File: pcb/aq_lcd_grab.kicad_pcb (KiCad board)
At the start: 2 copper layers, 52.1 x 60.8 mm, 2 parts, among them J1 Conn_01x39_Socket, J2 Conn_01x39_Socket

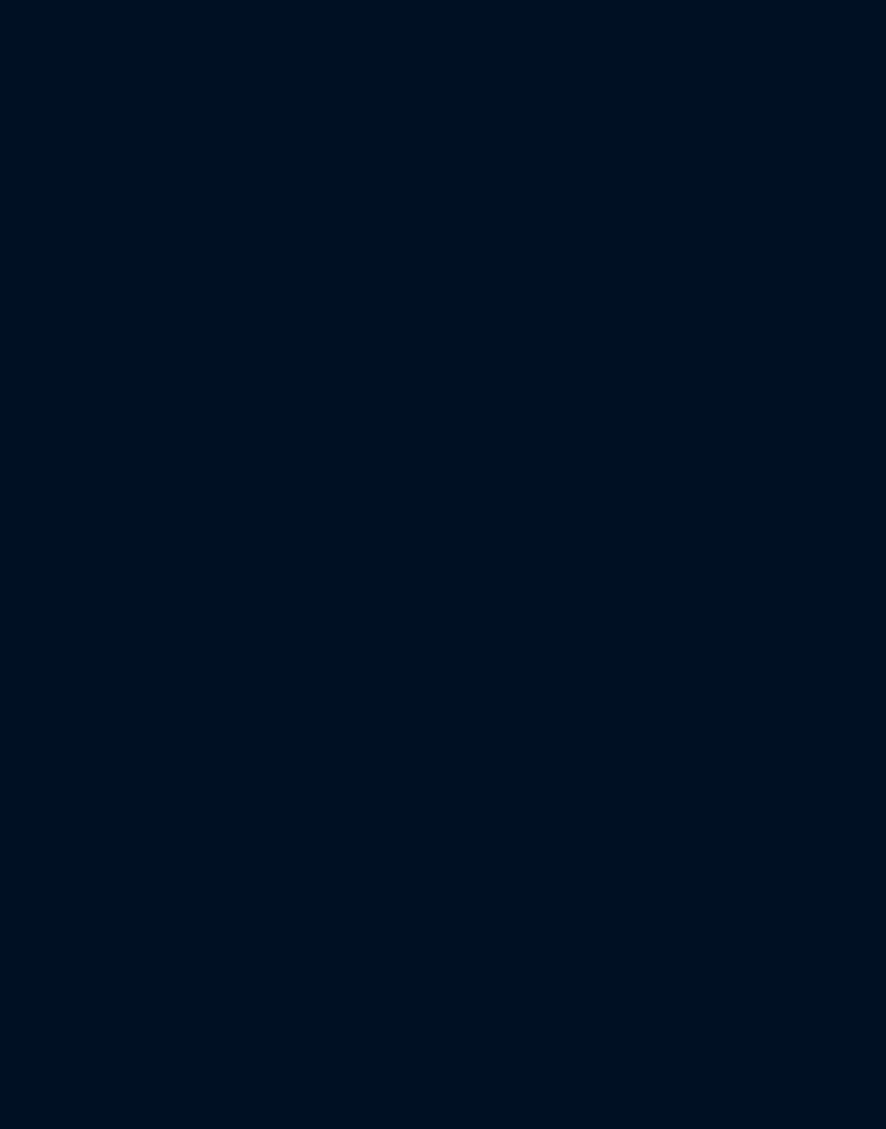
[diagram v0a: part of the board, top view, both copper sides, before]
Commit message: Add RP2350A to schematic, mirroring RPi minimal-board reference
Build out the SKiDL netlist with the RP2350A core and its supporting
components (decoupling, SMPS inductor, crystal, USB recovery header,
status LED, bring-up test points, 3-pin target power connector).

Components, values, and per-rail decoupling match Raspberry Pi's
official "RP2350 Minimal Board" KiCad design 1:1 where possible:
  - RP2350_60QFN symbol + custom QFN-60 ThermalVias footprint
  - L1 = 3.3 µH polarised AOTA-B201610S3R3-101-T on L_pol_2016
  - Y1 = ABM8-272-T3 12 MHz crystal, 15 pF load caps
  - C1/C2  ADC_AVDD bulk + HF (no ferrite, per RPi)
  - C5     VREG_VIN input (10 µF, 0805)
  - C6/C7  +1V1 bulk near L1 on the small_pads 0402 footprint
  - C8-C11 +1V1 HF decoupling
  - C9     VREG_AVDD decoupling
  - C12-C17 6× IOVDD decoupling (one cap per pin)
  - C18    extra +1V1 HF decoupling
  - C19/C20 QSPI_IOVDD / USB_OTP_VDD decoupling (our additions)
  - R2     XOUT damping (1 kΩ, in series between U1 pin 22 and Y1)
  - R4     RUN pull-up (1 kΩ)
  - R5     VREG_AVDD filter (33 Ω)
  - R7/R8  USB D±  series (27 Ω)
  - R20    QSPI_SD1 UART-boot pull-up (our addition)
  - R21    LED current limit (our addition)

Refdes mapping intentionally matches RPi's where the same component
plays the same role, so RPi's PCB layout for the U1 cluster can be
copy-pasted into ours.

Project-local sym-lib-table and fp-lib-table register the RPi symbol
file (MCU_RaspberryPi_RP2350.kicad_sym) and footprint library
(RP2350_60QFN_minimal.pretty/) — both copied from the upstream
Minimal-KiCAD.zip archive into pcb/ so the project builds standalone
without depending on the reference/ scratch folder.

.gitignore now skips reference/ (where the upstream archive is
unpacked locally for browsing in KiCanvas / KiCad).

docs/pcb_spec.md gains a Q7b section recording RPi's design-guide
recommendations (polarised inductor, ABM8 crystal, layout review).

Co-Authored-By: Claude Opus 4.7 (1M context) <noreply@anthropic.com>
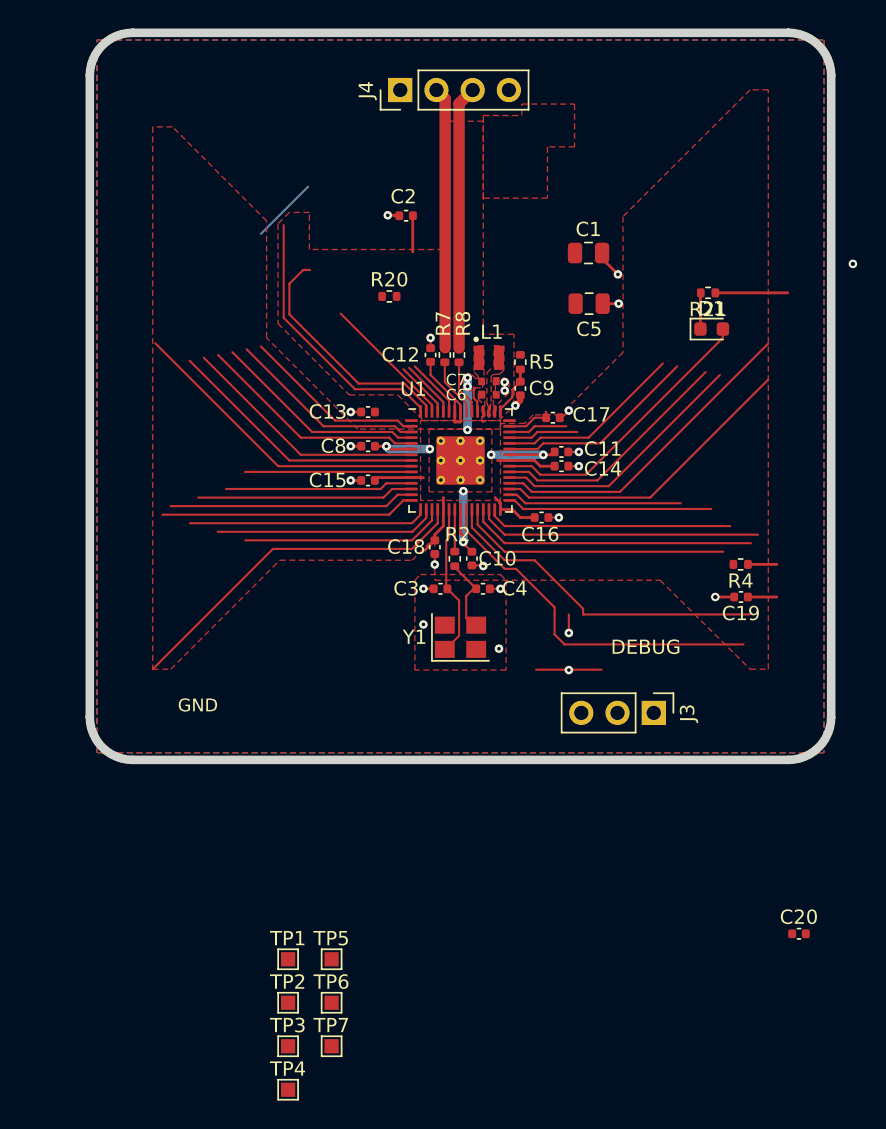
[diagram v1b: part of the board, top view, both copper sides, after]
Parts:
- added C1: 10u, Capacitor_SMD:C_0805_2012Metric, F.Cu at (230.9, 55.1)
- added C10: 4.7u, Capacitor_SMD:C_0402_1005Metric, F.Cu at (222.7, 76.6)
- added C11: 100n, Capacitor_SMD:C_0402_1005Metric, F.Cu at (229.0, 69.1)
- added C12: 100n, Capacitor_SMD:C_0402_1005Metric, F.Cu at (219.8, 62.3)
- added C13: 100n, Capacitor_SMD:C_0402_1005Metric, F.Cu at (215.4, 66.3)
- added C14: 100n, Capacitor_SMD:C_0402_1005Metric, F.Cu at (229.0, 70.1)
- added C15: 100n, Capacitor_SMD:C_0402_1005Metric, F.Cu at (215.4, 71.1)
- added C16: 100n, Capacitor_SMD:C_0402_1005Metric, F.Cu at (227.6, 73.7)
- added C17: 100n, Capacitor_SMD:C_0402_1005Metric, F.Cu at (228.4, 66.7)
- added C18: 100n, Capacitor_SMD:C_0402_1005Metric, F.Cu at (220.1, 75.8)
- added C19: 100n, Capacitor_SMD:C_0402_1005Metric, F.Cu at (241.6, 79.2)
- added C2: 100n, Capacitor_SMD:C_0402_1005Metric, F.Cu at (218.1, 52.5)
- added C20: 100n, Capacitor_SMD:C_0402_1005Metric, F.Cu at (245.6, 102.9)
- added C3: 15p, Capacitor_SMD:C_0402_1005Metric, F.Cu at (220.5, 78.7)
- added C4: 15p, Capacitor_SMD:C_0402_1005Metric, F.Cu at (223.5, 78.7)
- added C5: 10u, Capacitor_SMD:C_0805_2012Metric, F.Cu at (230.9, 58.7)
- added C6: 4.7u, RP2350_60QFN_minimal:C_0402_1005Metric_small_pads, F.Cu at (223.9, 65.1)
- added C7: 4.7u, RP2350_60QFN_minimal:C_0402_1005Metric_small_pads, F.Cu at (223.9, 64.1)
- added C8: 100n, Capacitor_SMD:C_0402_1005Metric, F.Cu at (215.4, 68.7)
- added C9: 4.7u, Capacitor_SMD:C_0402_1005Metric, F.Cu at (226.1, 64.6)
- added D1: GREEN, LED_SMD:LED_0603_1608Metric, F.Cu at (239.5, 60.5)
- added J3: Conn_01x03_Socket, Connector_PinHeader_2.54mm:PinHeader_1x03_P2.54mm_Vertical, F.Cu at (235.5, 87.4)
- added J4: Conn_01x04_Socket, Connector_PinHeader_2.54mm:PinHeader_1x04_P2.54mm_Vertical, F.Cu at (217.7, 43.7)
- added L1: 3.3u, RP2350_60QFN_minimal:L_pol_2016, F.Cu at (223.9, 62.5)
- added R2: 1k, Resistor_SMD:R_0402_1005Metric, F.Cu at (221.5, 76.6)
- added R20: 1k, Resistor_SMD:R_0402_1005Metric, F.Cu at (216.9, 58.2)
- added R21: 1k, Resistor_SMD:R_0402_1005Metric, F.Cu at (239.3, 57.9)
- added R4: 1k, Resistor_SMD:R_0402_1005Metric, F.Cu at (241.6, 77.0)
- added R5: 33, Resistor_SMD:R_0402_1005Metric, F.Cu at (226.1, 62.8)
- added R7: 27, Resistor_SMD:R_0402_1005Metric, F.Cu at (220.8, 62.3)
- added R8: 27, Resistor_SMD:R_0402_1005Metric, F.Cu at (221.8, 62.3)
- added TP1: TestPoint, TestPoint:TestPoint_Pad_1.0x1.0mm, F.Cu at (209.8, 104.7)
- added TP2: TestPoint, TestPoint:TestPoint_Pad_1.0x1.0mm, F.Cu at (209.8, 107.7)
- added TP3: TestPoint, TestPoint:TestPoint_Pad_1.0x1.0mm, F.Cu at (209.8, 110.8)
- added TP4: TestPoint, TestPoint:TestPoint_Pad_1.0x1.0mm, F.Cu at (209.8, 113.8)
- added TP5: TestPoint, TestPoint:TestPoint_Pad_1.0x1.0mm, F.Cu at (212.9, 104.7)
- added TP6: TestPoint, TestPoint:TestPoint_Pad_1.0x1.0mm, F.Cu at (212.9, 107.7)
- added TP7: TestPoint, TestPoint:TestPoint_Pad_1.0x1.0mm, F.Cu at (212.9, 110.8)
- added U1: RP2350_60QFN, RP2350_60QFN_minimal:RP2350-QFN-60-1EP_7x7_P0.4mm_EP3.4x3.4mm_ThermalVias, F.Cu at (221.9, 69.7)
- added Y1: ABM8-272-T3, Crystal:Crystal_SMD_3225-4Pin_3.2x2.5mm, F.Cu at (221.9, 82.1)
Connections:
- net /CS renamed CS
- net /DB0 renamed DB0
- net /DB1 renamed DB1
- net /DB10 renamed DB10
- net /DB11 renamed DB11
- net /DB12 renamed DB12
- net /DB13 renamed DB13
- net /DB14 renamed DB14
- net /DB15 renamed DB15
- net /DB2 renamed DB2
- net /DB3 renamed DB3
- net /DB4 renamed DB4
- net /DB5 renamed DB5
- net /DB6 renamed DB6
- net /DB7 renamed DB7
- net /DB8 renamed DB8
- net /DB9 renamed DB9
- net /DC renamed DC
- net /GND_1 renamed GND_1
- net /GND_18 renamed GND_18
- net /GND_19 renamed GND_19
- net /P20_RD renamed P20_RD
- net /P21 renamed P21
- net /P25 renamed P25
- net /P26 renamed P26
- net /P27 renamed P27
- net /P28 renamed P28
- net /P29 renamed P29
- net /P30 renamed P30
- net /P31 renamed P31
- net /P32 renamed P32
- net /P34 renamed P34
- net /P38 renamed P38
- net /P39 renamed P39
- net /VCC_33 renamed VCC_33
- net /VCC_35 renamed VCC_35
- net /VCC_36 renamed VCC_36
- net /VCC_37 renamed VCC_37
- net /WR renamed WR
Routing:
- net (no net): track 0.00 -> 372.7 mm, vias 0 -> 1
- net +3V3: track 0.00 -> 41.7 mm
- net GND: track 0.00 -> 40.2 mm, vias 0 -> 22
- net SWCLK: track 0.00 -> 25.3 mm
- net +1V1: track 0.00 -> 25.0 mm, vias 0 -> 9
- net SWDIO: track 0.00 -> 23.5 mm
- net USB_DP: track 0.00 -> 23.0 mm, vias 0 -> 1
- net GPIO22: track 0.00 -> 22.7 mm
- net GPIO21: track 0.00 -> 21.8 mm
- net LED_STATUS: track 0.00 -> 19.8 mm
- net RUN: track 0.00 -> 19.1 mm
- net USB_DM: track 0.00 -> 18.5 mm
- net GPIO23: track 0.00 -> 18.2 mm
- net N$1: track 0.00 -> 16.7 mm
- net GPIO19: track 0.00 -> 14.4 mm
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- added copper zone on F.Cu, net +1V1
- added copper zone on F.Cu, net +3V3
- added copper zone on B.Cu, net GND
- added copper zone on F.Cu, net GND
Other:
- board size 52.1 x 60.8 mm -> 170.4 x 70.2 mm
- rule pad_to_mask_clearance: 0 -> 0.051
- board text added: "DEBUG"
- board text added: "GND"

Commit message: Wire Xiao ESP32-C6 into netlist (UART boot loader + PIC32 reset)
Adds U2 (Xiao ESP32-C6 DIP module) to the SKiDL netlist with the
core control signals defined in the PCB spec:

  - GPIO16 / GPIO17 (UART0 TX/RX) -> RP2350 QSPI_SD3 / SD2 for 1 Mbaud
    UART boot loading; remuxes to RP2350 PL011 UART0 (F11 alt) at runtime
  - GPIO0  -> RP2350 RUN (push-pull; R4 supplies the pull-up)
  - GPIO1  -> PIC32 reset on J3 pin 3 (open-drain; main board pull-up)
  - 3V3 backfeed on pad 12 (bypasses Xiao's onboard LDO)
  - 5V / VBUS tied to the USB recovery header rail

Adds 22 uF + 100 uF bulk caps at the Xiao 3V3 input (C30/C31) to
absorb WiFi TX transients locally instead of pushing them onto the
target 3V3 rail (spec Q6/Q7 mitigation).

Footprint comes from a locally-tweaked SnapEDA Xiao-ESP32-C6-DIP
shipped as a project-local pretty library, mirroring the way the
RP2350 minimal-board parts are vendored.

J3 pin 3 graduates from "reserved/floating" to a real PIC32_RESET
net now that there's an ESP32 GPIO to drive it.

Co-Authored-By: Claude Opus 4.7 (1M context) <noreply@anthropic.com>
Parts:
- removed C19, C20: 100n, Capacitor_SMD:C_0402_1005Metric
- removed TP6, TP7: TestPoint, TestPoint:TestPoint_Pad_1.0x1.0mm
- added C30: 22u, Capacitor_SMD:C_0805_2012Metric, F.Cu at (256.7, 89.2)
- added C31: 100u, Capacitor_SMD:C_1206_3216Metric, F.Cu at (257.3, 86.0)
- added J5: Conn_01x03_Pin, Connector_PinHeader_2.54mm:PinHeader_1x03_P2.54mm_Vertical, F.Cu at (231.9, 86.6)
- added U2: Conn_01x14, esp32c6:XIAO-ESP32-C6-DIP, B.Cu at (221.0, 68.6)
- moved J1 107.8 mm to (174.5, 136.9), turned to 0 degrees
- moved J2 57.3 mm to (173.9, 106.7), turned to 180 degrees
- moved J3 24.1 mm to (211.3, 86.9)
- moved TP5 12.2 mm to (224.2, 100.0)
- moved TP2 11.2 mm to (217.4, 99.4)
- moved TP3 9.06 mm to (205.4, 102.8)
- moved TP4 8.50 mm to (210.1, 105.3)
- moved TP1 8.12 mm to (205.9, 97.5)
- moved C17 1.59 mm to (227.1, 67.6)
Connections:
- J3 pad 3: (no net) -> PIC32_RESET
- TP1 pad 1: SWCLK -> GPIO19
- TP2 pad 1: SWDIO -> GPIO20
- TP3 pad 1: GPIO19 -> GPIO21
- TP4 pad 1: GPIO20 -> GPIO22
- TP5 pad 1: GPIO21 -> GPIO23
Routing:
- net (no net): track 372.7 -> 197.2 mm, vias 1 -> 0
- net GND: track 40.2 -> 106.6 mm
- net GND_1: track 65.9 -> 2.80 mm
- net DB1: track 59.2 -> 3.52 mm
- net P39: track 57.1 -> 2.80 mm
- net DB0: track 53.9 -> 0.00 mm
- net PIC32_RESET: track 0.00 -> 51.9 mm
- net P38: track 51.6 -> 0.02 mm
- net DB3: track 62.7 -> 12.6 mm
- net DB2: track 51.3 -> 2.10 mm
- net VCC_37: track 61.1 -> 14.2 mm
- net VCC_36: track 50.0 -> 4.52 mm
- net DB5: track 55.5 -> 10.9 mm
- net DB4: track 49.5 -> 5.74 mm
- net VCC_35: track 53.9 -> 12.5 mm
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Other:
- board size 170.4 x 70.2 mm -> 95.5 x 102 mm
- copper layers 2 -> 4
- board text removed: "GND"

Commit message: Match RP2350 decoupling network exactly to RPi reference
Rewrites the decoupling block to mirror the Raspberry Pi RP2350
"Minimal Board" reference design (reference/RP2350A_Minimal/) 1:1.
The previous version had drifted in several ways while I wired in
the ESP32 and tried to "approximate" the reference roles -- enough
mistakes accumulated that an audit and rewrite was simpler than
patching individual pins.

Bugs fixed:
  - Pad 6 (DVDD #1) was dangling; now tied to +1V1.
  - Pad 23 (DVDD #2) was on VREG_AVDD (via the decouple() helper);
    now on +1V1 alongside pads 6 and 39.
  - C18 was a 100 nF on VREG_AVDD; reference puts it on +3V3 as a
    generic bypass. VREG_AVDD has no HF cap in the reference, only
    the 4.7 µF C9.
  - C6 was on +1V1; reference puts it on +3V3 as the pre-L1 input
    bulk near VREG_VIN.
  - C9 was bridged between VREG_AVDD and pad 23 (via decouple()
    helper). C9 is a standalone rail cap on VREG_AVDD in the
    reference, untouched by any chip pad.
  - L1 pin 1/2 were swapped relative to the reference. Pin 1 is
    the +1V1 (output) side, pin 2 the VREG_LX (switching) side --
    matters for the silkscreen dot on the polarised AOTA-B201610S3R3.
  - C19 (10 µF on +3V3, rail bulk near U1) was missing entirely.

Refdes that don't appear in our design (because we don't have RPi's
onboard 3V3 regulator or QSPI flash): C1, C2, C5. Our 10 µF +3V3
bulk now lives on C19 (matching the reference), not C5 or C1.

All other rails (XIN/XOUT/+3V3/+1V1/VREG_AVDD/VREG_LX) now match
the reference netlist node-for-node.

Includes the layout-side changes (4-layer stackup, test point
repositioning, footprint imports for the ESP32 + new caps) that
piled up in the .kicad_pcb during this work.

Co-Authored-By: Claude Opus 4.7 (1M context) <noreply@anthropic.com>
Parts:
- removed C1, C5: 10u, Capacitor_SMD:C_0805_2012Metric
- removed C2: 100n, Capacitor_SMD:C_0402_1005Metric
- added C17: 100n, Capacitor_SMD:C_0402_1005Metric, F.Cu at (53.9, 57.0)
- added C19: 10u, Capacitor_SMD:C_0805_2012Metric, F.Cu at (40.0, 49.8)
- moved R4 203.2 mm to (40.6, 46.8), turned to 0 degrees
- moved D1 196.9 mm to (42.7, 63.3), turned to 180 degrees
- moved R21 196.5 mm to (42.9, 65.9), turned to 0 degrees
- moved TP2 189.5 mm to (32.0, 59.9)
- moved C31 188.4 mm to (71.0, 113.5)
- moved J5 184.4 mm to (53.3, 40.6), turned to 0 degrees
- moved TP4 183.9 mm to (33.3, 54.6)
- moved C14 176.5 mm to (53.2, 53.7), turned to 180 degrees
- moved C11 176.3 mm to (53.2, 54.7), turned to 180 degrees
- moved C16 174.2 mm to (55.0, 49.9), turned to 180 degrees
- moved C9 170.3 mm to (55.9, 59.2), turned to 90 degrees
- moved R5 170.2 mm to (55.9, 61.0), turned to 90 degrees
- moved C4 168.1 mm to (58.7, 45.1), turned to 180 degrees
- moved Y1 166.6 mm to (60.3, 41.7), turned to 180 degrees
- moved C10 165.8 mm to (59.5, 47.2), turned to 90 degrees
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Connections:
- C6 pad 1: +1V1 -> +3V3
- L1 pad 1: VREG_LX -> +1V1
- L1 pad 2: +1V1 -> VREG_LX
- U1 pad 10: (no net) -> DB0
- U1 pad 12: (no net) -> DB1
- U1 pad 13: (no net) -> DB3
- U1 pad 14: (no net) -> DB5
- U1 pad 15: (no net) -> DB7
- U1 pad 16: (no net) -> DB9
- U1 pad 17: (no net) -> DB11
- U1 pad 18: (no net) -> DB13
- U1 pad 19: (no net) -> DB15
- U1 pad 2: (no net) -> DB14
- U1 pad 23: VREG_AVDD -> +1V1
- U1 pad 27: (no net) -> DC
- U1 pad 28: (no net) -> CS
- U1 pad 29: (no net) -> WR
- U1 pad 3: (no net) -> DB12
- U1 pad 4: (no net) -> DB10
- U1 pad 46: +3V3 -> VREG_AVDD
- U1 pad 5: (no net) -> DB8
- U1 pad 6: (no net) -> +1V1
- U1 pad 7: (no net) -> DB6
- U1 pad 8: (no net) -> DB4
- U1 pad 9: (no net) -> DB2
- U2 pad 1: RUN -> (no net)
- U2 pad 10: (no net) -> PIC32_RESET
- U2 pad 2: PIC32_RESET -> (no net)
- U2 pad 9: (no net) -> RUN
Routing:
- net (no net): track 197.2 -> 11.1 mm
- net GND: track 106.6 -> 12.0 mm, vias 22 -> 21
- net PIC32_RESET: track 51.9 -> 0.00 mm
- net DB1: track 3.52 -> 53.2 mm, vias 2 -> 3
- net DB0: track 0.00 -> 46.4 mm, vias 0 -> 2
- net DB2: track 2.10 -> 43.5 mm, vias 0 -> 2
- net DB3: track 12.6 -> 52.1 mm, vias 2 -> 3
- net DB5: track 10.9 -> 50.2 mm, vias 2 -> 3
- net DB4: track 5.74 -> 45.0 mm, vias 0 -> 2
- net UART_RP_TX: track 34.7 -> 0.46 mm
- net GND_1: track 2.80 -> 36.9 mm
- net P39: track 2.80 -> 36.1 mm
- net DB6: track 9.62 -> 41.9 mm, vias 0 -> 2
- net DB9: track 18.7 -> 49.2 mm, vias 2 -> 3
- net DB8: track 13.5 -> 43.2 mm, vias 0 -> 2
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- added copper zone on F.Cu, net VREG_LX
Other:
- board size 95.5 x 102 mm -> 32 x 50 mm
